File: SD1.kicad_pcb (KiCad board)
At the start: 2 copper layers, 76.2 x 38.1 mm, 145 parts, among them J101 HR861153C, J102 10118194-0001LF, J107 FPC PMS, J401 Conn_01x11, J403 FTDI_TTL_Cable, Q1 FDC2512, Q101 BSS138, Q102 PDTC114EU,115, SW103 Multidirection_Switch, SW104 Multifunction_Switch, SW401 PTS810, U101 TLV70233_SOT23-5, U102 ER-TFTM028-4, U103 CP2102N-A02-GQFN28R, U104 CC2652P, U105 W5500, U107 MCP23017, U3 TL431D, Y101 25MHz

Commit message: PoE layout
Changed opto and fixed ref diode footprint/symbol
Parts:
- removed C105, C106: 1u, Capacitor_SMD:C_0603_1608Metric
- removed D1, D2: MURA120, Diode_SMD:D_SMA
- removed R17: 39.2k, Resistor_SMD:R_0603_1608Metric
- removed R18: 392k, Resistor_SMD:R_0603_1608Metric
- removed SW104: Multifunction_Switch, mylib:K1-1508SA-01
- removed U101: TLV70233_SOT23-5, Package_TO_SOT_SMD:SOT-23-5
- removed U102: ER-TFTM028-4, mylib:ER-TFTM028-4
- added C109: 0.1u, Capacitor_SMD:C_0603_1608Metric, F.Cu at (132.9, 152.0)
- added C110: 0.1u, Capacitor_SMD:C_0603_1608Metric, F.Cu at (43.3, 117.8)
- added C112: 0.1u, Capacitor_SMD:C_0603_1608Metric, F.Cu at (43.3, 110.3)
- added C114: 10u, Capacitor_SMD:C_0603_1608Metric, F.Cu at (47.3, 113.7)
- added C301: 0.1u, Capacitor_SMD:C_0603_1608Metric, F.Cu at (55.4, 157.6)
- added C302: 0, Capacitor_SMD:C_0603_1608Metric, F.Cu at (52.0, 157.9)
- added C501: 1u, Capacitor_SMD:C_0603_1608Metric, F.Cu at (113.1, 155.3)
- added C502: 1u, Capacitor_SMD:C_0603_1608Metric, F.Cu at (113.6, 157.8)
- added C504: 0.1u, Capacitor_SMD:C_0603_1608Metric, F.Cu at (117.6, 156.6)
- added C505: 0.1u, Capacitor_SMD:C_0603_1608Metric, F.Cu at (113.6, 160.3)
- added C506: 10u, Capacitor_SMD:C_0603_1608Metric, F.Cu at (123.6, 152.0)
- added C507: 10u, Capacitor_SMD:C_0603_1608Metric, F.Cu at (117.6, 159.1)
- added C508: 1u, Capacitor_SMD:C_0603_1608Metric, F.Cu at (121.6, 156.6)
- added C601: 0.1u, Capacitor_SMD:C_0603_1608Metric, F.Cu at (31.0, 181.9)
- added C701: 10u, Capacitor_SMD:C_0603_1608Metric, F.Cu at (20.3, 148.4)
- added C704: 10u, Capacitor_SMD:C_0603_1608Metric, F.Cu at (16.3, 150.9)
- added C705: 10u, Capacitor_SMD:C_0603_1608Metric, F.Cu at (22.5, 144.8)
- added C706: 100p, Capacitor_SMD:C_0603_1608Metric, F.Cu at (16.3, 148.4)
- added C707: 47u, Capacitor_SMD:C_1210_3225Metric, F.Cu at (13.3, 143.6)
- added C708: 47u, Capacitor_SMD:C_1210_3225Metric, F.Cu at (11.5, 149.9)
- added C709: 100p, Capacitor_SMD:C_0603_1608Metric, F.Cu at (27.6, 135.5)
- added C710: 10u, Capacitor_SMD:C_0603_1608Metric, F.Cu at (31.6, 135.5)
- added C711: 10u, Capacitor_SMD:C_0603_1608Metric, F.Cu at (27.8, 138.0)
- added D3: BAS16, Diode_SMD:D_SOT-23_ANK, F.Cu at (228.2, 81.7)
- added D301: MURA120, Diode_SMD:D_SMA, F.Cu at (210.2, 25.1)
- added D302: MURA120, Diode_SMD:D_SMA, F.Cu at (214.7, 25.1)
- added D303: MURA120, Diode_SMD:D_SMA, F.Cu at (197.2, 25.2)
- added D304: MURA120, Diode_SMD:D_SMA, F.Cu at (201.0, 25.2)
- added D501: Photodiode alt, LED_THT:LED_D3.0mm_Clear, F.Cu at (107.4, 160.0)
- added D7: LED_ALT, LED_SMD:LED_0603_1608Metric, F.Cu at (261.6, 78.8)
- added D701: BAS16, Diode_SMD:D_SOT-23_ANK, F.Cu at (5.78, 149.4)
- added FB102: Ferrite_Bead_Small, Inductor_SMD:L_0603_1608Metric, F.Cu at (47.2, 106.2)
- added FB2: 10, Resistor_SMD:R_0603_1608Metric, F.Cu at (201.8, 76.6)
- added FB3: 10, Resistor_SMD:R_0603_1608Metric, F.Cu at (201.8, 81.8)
- added FB301: Ferrite_Bead_Small, Inductor_SMD:L_0603_1608Metric, F.Cu at (40.2, 135.5)
- added FB501: Ferrite_Bead_Small, Inductor_SMD:L_0603_1608Metric, F.Cu at (107.1, 187.4)
- added J103: JST ZH 1.5mm 1x5, mylib:JST-ZR-B5B-SM4-TFLFSN_1x05-1MP_P1.5mm_Vertical, F.Cu at (156.8, 143.0)
- added J301: PJ-102AH, Connector_BarrelJack:BarrelJack_CUI_PJ-102AH_Horizontal, F.Cu at (213.0, 19.2)
- added J302: PJ-102AH, Connector_BarrelJack:BarrelJack_CUI_PJ-102AH_Horizontal, F.Cu at (199.6, 19.0)
- added J303: Conn_01x02, Connector_PinSocket_2.54mm:PinSocket_1x02_P2.54mm_Vertical, F.Cu at (205.4, 69.0)
- added J304: Conn_01x02, Connector_PinSocket_2.54mm:PinSocket_1x02_P2.54mm_Vertical, F.Cu at (88.3, 107.2)
- added J402: Conn_ARM_JTAG_SWD_10, mylib:PinHeader_2x05_P1.27mm_Thin_Shrouded_Vertical_SMD, F.Cu at (57.6, 136.0)
- added J801: Conn_01x02, Connector_PinHeader_2.54mm:PinHeader_1x02_P2.54mm_Vertical, F.Cu at (12.8, 136.6)
- added JP301: Jumper_NO_Small, Jumper:SolderJumper-2_P1.3mm_Open_TrianglePad1.0x1.5mm, F.Cu at (263.6, 75.4)
- added JP401: Jumper_NO_Small, Connector_PinHeader_2.54mm:PinHeader_1x02_P2.54mm_Vertical, F.Cu at (64.8, 134.1)
- added JP701: Jumper_NO_Small, Jumper:SolderJumper-2_P1.3mm_Open_TrianglePad1.0x1.5mm, F.Cu at (18.3, 145.3)
- added JP702: Jumper_3_Bridged12, Jumper:SolderJumper-3_P1.3mm_Bridged12_Pad1.0x1.5mm, F.Cu at (17.9, 136.0)
- added L1: 4.7u, Inductor_SMD:L_Taiyo-Yuden_MD-4040, F.Cu at (218.3, 81.1)
- added L701: 1u, mylib:L_Wuerth_HCI-5040, F.Cu at (6.68, 144.4)
- added L702: 1u, mylib:L_Wuerth_HCI-5040, F.Cu at (6.68, 137.6)
- added Q301: DMMT5401, Package_TO_SOT_SMD:SOT-23-6, F.Cu at (267.4, 75.4)
- added Q302: DMMT5401, Package_TO_SOT_SMD:SOT-23-6, F.Cu at (267.4, 79.2)
- added Q801: DMMT5401, Package_TO_SOT_SMD:SOT-23-6, F.Cu at (23.2, 136.6)
- added Q802: DMMT5401, Package_TO_SOT_SMD:SOT-23-6, F.Cu at (18.5, 141.2)
- added Q803: DMMT5401, Package_TO_SOT_SMD:SOT-23-6, F.Cu at (23.4, 141.2)
- added R107: 47.5k, Resistor_SMD:R_0603_1608Metric, F.Cu at (95.3, 152.4)
- added R114: 10k, Resistor_SMD:R_0603_1608Metric, F.Cu at (47.3, 111.2)
- added R115: 10k, Resistor_SMD:R_0603_1608Metric, F.Cu at (43.3, 115.3)
- added R116: 10k, Resistor_SMD:R_0603_1608Metric, F.Cu at (43.3, 112.8)
- added R117: 10k, Resistor_SMD:R_0603_1608Metric, F.Cu at (47.3, 108.7)
- added R301: 0, Resistor_SMD:R_0603_1608Metric, F.Cu at (58.0, 152.4)
- added R302: 499k, Resistor_SMD:R_0603_1608Metric, F.Cu at (52.0, 160.4)
- added R303: 392k, Resistor_SMD:R_0603_1608Metric, F.Cu at (193.8, 22.2)
- added R304: 39.2k, Resistor_SMD:R_0603_1608Metric, F.Cu at (192.0, 20.6)
- added R305: 10k, Resistor_SMD:R_0603_1608Metric, F.Cu at (264.8, 78.8)
- added R306: 47.5k, Resistor_SMD:R_0603_1608Metric, F.Cu at (270.0, 78.8)
- added R307: 100k, Resistor_SMD:R_0603_1608Metric, F.Cu at (260.2, 82.0)
- added R308: 100k, Resistor_SMD:R_0603_1608Metric, F.Cu at (263.2, 82.0)
- added R501: 1M, Resistor_SMD:R_0603_1608Metric, F.Cu at (117.6, 161.6)
- added R601: 10k, Resistor_SMD:R_0603_1608Metric, F.Cu at (31.0, 184.4)
- added R602: 10k, Resistor_SMD:R_0603_1608Metric, F.Cu at (35.0, 181.9)
- added R603: 10k, Resistor_SMD:R_0603_1608Metric, F.Cu at (35.0, 184.4)
- added R702: 732k, Resistor_SMD:R_0603_1608Metric, F.Cu at (24.3, 149.8)
- added R703: 392k, Resistor_SMD:R_0603_1608Metric, F.Cu at (30.5, 143.1)
- added R704: 100k, Resistor_SMD:R_0603_1608Metric, F.Cu at (31.8, 140.5)
- added R705: 100k, Resistor_SMD:R_0603_1608Metric, F.Cu at (24.3, 147.3)
- added R801: 100k, Resistor_SMD:R_0603_1608Metric, F.Cu at (31.8, 138.0)
- added R802: 10k, Resistor_SMD:R_0603_1608Metric, F.Cu at (20.3, 150.9)
- added R803: 47.5k, Resistor_SMD:R_0603_1608Metric, F.Cu at (26.5, 144.8)
- added R804: 59k, Resistor_SMD:R_0603_1608Metric, F.Cu at (27.8, 140.5)
- added T1: HR051067, mylib:HR051067, F.Cu at (238.2, 75.4)
- added TP301: TestPoint, TestPoint:TestPoint_Pad_D1.0mm, F.Cu at (106.6, 196.5)
- added TP302: TestPoint, TestPoint:TestPoint_Pad_D1.0mm, F.Cu at (109.6, 196.5)
- added TP303: TestPoint, TestPoint:TestPoint_Pad_D1.0mm, F.Cu at (112.7, 196.5)
- added TP304: TestPoint, Connector_PinSocket_2.54mm:PinSocket_1x01_P2.54mm_Vertical, F.Cu at (258.7, 79.4)
- added TP501: TestPoint, TestPoint:TestPoint_Pad_D1.0mm, F.Cu at (106.6, 190.1)
- added TP502: TestPoint, TestPoint:TestPoint_Pad_D1.0mm, F.Cu at (110.6, 187.6)
- added U106: EKMC1691111, mylib:EKM, F.Cu at (84.2, 159.2)
- added U108: BME280, Package_LGA:Bosch_LGA-8_2.5x2.5mm_P0.65mm_ClockwisePinNumbering, F.Cu at (43.2, 107.0)
- added U109: SCD30, mylib:SCD30, F.Cu at (7.15, 106.9)
- added U2: TPS23753A, Package_SO:TSSOP-14_4.4x5mm_P0.65mm, B.Cu at (211.6, 73.6)
- added U301: 110-102, mylib:SPEC_110-102, F.Cu at (37.5, 163.7)
- added U302: LMP91000, Package_SON:WSON-14-1EP_4.0x4.0mm_P0.5mm_EP2.6x2.6mm, F.Cu at (53.0, 153.9)
- added U4: TCMT1107, Package_SO:SOIC-4_4.55x2.6mm_P1.27mm, F.Cu at (238.2, 67.0)
- added U501: TLV70018, Package_TO_SOT_SMD:SOT-353_SC-70-5, F.Cu at (119.1, 153.0)
- added U502: ADPD188BI, mylib:ADPD188BI, F.Cu at (108.4, 154.0)
- added U601: CCS811, Package_LGA:AMS_LGA-10-1EP_2.7x4mm_P0.6mm, F.Cu at (26.9, 183.4)
- added U701: TPS61022, mylib:Texas_VQFN-HR-7, F.Cu at (28.4, 147.8)
- added U702: TLV62585, Package_TO_SOT_SMD:SOT-563, F.Cu at (32.2, 145.9)
- C141: footprint Capacitor_SMD:C_1206_3216Metric -> Capacitor_SMD:C_0603_1608Metric
- C160: value 10n -> 8.2nF
- C24, C26, C32, C33, C34, C35, C36, C37, D6, R19, R20, R22, R23, R24, R25, R26, R27, R28, R29, R30, R32, R34, R35, R36, R37: moved to B.Cu
- FB101: value 470 -> Ferrite_Bead_Small
- Q1: value FDC2512 -> FDT86244; footprint Package_TO_SOT_SMD:SuperSOT-6 -> Package_TO_SOT_SMD:SOT-223-3_TabPin2
- R31: footprint Resistor_SMD:R_0805_2012Metric -> Resistor_SMD:R_0603_1608Metric
- U3: value TL431D -> TL431A; footprint Package_SO:SOIC-8_3.9x4.9mm_P1.27mm -> Package_TO_SOT_SMD:SOT-23; moved to B.Cu
- moved C28 107.2 mm to (259.2, 74.0), turned to 90 degrees
- moved D4 96.6 mm to (251.6, 78.6), turned to 180 degrees
- moved C35 95.8 mm to (253.8, 75.3), turned to 180 degrees
- moved C29 95.3 mm to (251.8, 72.7), turned to 90 degrees
- moved D6 95.1 mm to (249.0, 74.8), turned to 180 degrees
- moved R26 94.3 mm to (232.1, 74.4)
- moved U3 93.0 mm to (253.6, 71.1)
- moved C33 90.2 mm to (253.8, 73.8), turned to 180 degrees
- moved R27 89.0 mm to (249.2, 77.4), turned to 180 degrees
- moved R37 86.2 mm to (256.1, 70.8), turned to 90 degrees
- moved R24 85.2 mm to (256.1, 76.8), turned to 270 degrees
- moved C24 84.7 mm to (253.4, 79.4), turned to 180 degrees
- moved C27 83.0 mm to (255.0, 72.7), turned to 90 degrees
- moved C32 81.0 mm to (233.6, 71.8), turned to 180 degrees
- moved R31 77.7 mm to (263.2, 78.8), turned to 270 degrees
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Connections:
- net /Eth + PoE/PoE Flyback/5V_SYS renamed /Eth + PoE/PoE Flyback/5V_Main
- net /WMCU_SWO renamed /WMCU_RTS
- C23 pad 1: (no net) -> Net-(C23-Pad1)
- J107 pad 3: (no net) -> /EXT_Sleep
- J107 pad 4: (no net) -> I2C_SCL
- J107 pad 5: (no net) -> I2C_SDA
- J403 pad 3: (no net) -> Net-(J403-Pad3)
- LS101 pad 1: /5V_USB -> +3V3
- Q1 pad 2: Net-(Q1-Pad1) -> Net-(Q1-Pad2)
- R108 pad 2: /5V_USB -> +3V3
- R111 pad 1: (no net) -> /I_LED_R
- R112 pad 1: (no net) -> /I_LED_G
- R113 pad 1: (no net) -> /I_LED_B
- R19 pad 2: (no net) -> Net-(R19-Pad2)
- R21 pad 1: (no net) -> Net-(R21-Pad1)
- R21 pad 2: (no net) -> Net-(D3-Pad2)
- R22 pad 1: (no net) -> Net-(J303-Pad2)
- R23 pad 1: (no net) -> Net-(R23-Pad1)
- R25 pad 1: Net-(Q1-Pad3) -> Net-(Q1-Pad1)
- R25 pad 2: (no net) -> Net-(R25-Pad2)
- R26 pad 1: Net-(Q1-Pad1) -> Net-(Q1-Pad2)
- R27 pad 2: (no net) -> Net-(R27-Pad2)
- R30 pad 1: Net-(Q1-Pad4) -> Net-(Q1-Pad3)
- R30 pad 2: (no net) -> Net-(R30-Pad2)
- R31 pad 2: (no net) -> Net-(D7-Pad2)
- R32 pad 1: (no net) -> Net-(R32-Pad1)
- R33 pad 1: Net-(Q1-Pad4) -> Net-(Q1-Pad3)
- SW103 pad 1: (no net) -> /Multi_A
- SW103 pad 2: (no net) -> /Multi_B
- SW103 pad 3: (no net) -> /Multi_C
- SW103 pad 4: (no net) -> /Multi_Press
- SW103 pad 5: (no net) -> GND
- SW103 pad 6: (no net) -> /Multi_D
- U103 pad 25: /DIO13_TXD -> /DIO12_RXD
- U103 pad 26: /DIO12_RXD -> /DIO13_TXD
- U104 pad 1: (no net) -> I2C_SDA
- U104 pad 14: (no net) -> GND
- U104 pad 16: /DIO16_TDO -> (no net)
- U104 pad 17: /DIO17_TDI -> /DIO16_TDO
- U104 pad 18: (no net) -> /DIO17_TDI
- U104 pad 21: (no net) -> I2C_SCL
- U104 pad 24: (no net) -> /CO_ADC
- U104 pad 25: (no net) -> 5V_MainDet
- U104 pad 4: (no net) -> SPI_MISO
- U104 pad 5: (no net) -> SPI_MOSI
- U104 pad 6: (no net) -> SPI_SCK
- U105 pad 37: (no net) -> /~ETH_RST
- U107 pad 12: (no net) -> I2C_SCL
- U107 pad 13: (no net) -> I2C_SDA
- U107 pad 21: (no net) -> /I_LED_R
- U107 pad 22: (no net) -> /I_LED_G
- U107 pad 23: (no net) -> /I_LED_B
- U107 pad 24: (no net) -> /Multi_A
- U107 pad 25: (no net) -> /Multi_B
- U107 pad 26: (no net) -> /Multi_C
- U107 pad 27: (no net) -> /Multi_D
- U107 pad 28: (no net) -> /Multi_Press
- U107 pad 3: (no net) -> /LCD_DC
- U107 pad 4: (no net) -> /FONT_CS
- U107 pad 6: (no net) -> /~ETH_RST
- U107 pad 7: (no net) -> /VOC_INT
- U107 pad 8: (no net) -> /EXT_Sleep
- U3 pad 2: GND -> Net-(C33-Pad1)
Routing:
- net GNDD: track 0.00 -> 104.7 mm, vias 0 -> 21
- net GND: track 55.4 -> 114.0 mm, vias 8 -> 10
- net Net-(C37-Pad2): track 0.00 -> 26.1 mm, vias 0 -> 1
- net Net-(C21-Pad1): track 0.00 -> 25.6 mm, vias 0 -> 1
- net /Eth + PoE/PoE Flyback/VSS_FILT: track 0.00 -> 22.9 mm, vias 0 -> 2
- net Net-(C25-Pad1): track 0.00 -> 20.8 mm, vias 0 -> 1
- net +5V: track 0.00 -> 20.0 mm
- net Net-(C33-Pad2): track 0.00 -> 19.7 mm, vias 0 -> 1
- net /Eth + PoE/PoE Flyback/5V_Main: track 0.00 -> 18.4 mm, vias 0 -> 2
- net Net-(C23-Pad1): track 0.00 -> 16.3 mm
- net Net-(Q1-Pad1): track 0.00 -> 14.7 mm, vias 0 -> 1
- net Net-(R27-Pad2): track 0.00 -> 14.2 mm, vias 0 -> 1
- net Net-(D6-Pad2): track 0.00 -> 13.9 mm
- net 5V_MainDet: track 0.00 -> 13.6 mm
- net /Eth + PoE/PoE Flyback/VP: track 13.1 -> 25.9 mm
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- added copper zone on F.Cu, net /Eth + PoE/PoE Flyback/5V_Main
- added copper zone on B.Cu, net /Eth + PoE/PoE Flyback/VSS_FILT
- added copper zone on B.Cu, net GNDD
- added copper zone on F.Cu, net GNDD
- added copper zone on B.Cu, net Net-(C21-Pad1)
- added copper zone on F.Cu, net Net-(C21-Pad1)
- added copper zone on F.Cu, net Net-(C23-Pad1)
- added copper zone on F.Cu, net Net-(D4-Pad2)
- added copper zone on F.Cu, net Net-(JP301-Pad2)
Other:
- board size 76.2 x 38.1 mm -> 176.1 x 41.3 mm

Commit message: Layout for Smoke and Reference Indicators for PoE
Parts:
- C501, C502, FB501, U501: moved to B.Cu
- moved FB501 147.7 mm to (54.5, 49.4), turned to 180 degrees
- moved D501 141.5 mm to (41.9, 34.6)
- moved TP501 139.0 mm to (75.7, 54.6)
- moved TP502 135.3 mm to (75.7, 56.9)
- moved C505 127.7 mm to (54.7, 47.0)
- moved C507 126.2 mm to (49.1, 53.1), turned to 180 degrees
- moved C504 125.0 mm to (54.7, 48.6)
- moved C508 124.9 mm to (55.9, 50.4)
- moved R501 124.0 mm to (58.8, 52.5)
- moved C506 122.5 mm to (49.1, 54.6), turned to 180 degrees
- moved C502 120.4 mm to (56.8, 51.7), turned to 90 degrees
- moved U501 120.3 mm to (54.4, 51.7)
- moved C501 120.2 mm to (51.9, 51.8), turned to 90 degrees
- moved U502 113.4 mm to (54.6, 54.1)
- moved C401 57.3 mm to (98.8, 88.1), turned to 180 degrees
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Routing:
- net GND: track 114.0 -> 145.5 mm, vias 10 -> 12
- net Net-(D501-Pad1): track 0.00 -> 23.4 mm
- net Net-(D501-Pad2): track 0.00 -> 21.1 mm
- net Net-(TP502-Pad1): track 0.00 -> 20.2 mm
- net Net-(TP501-Pad1): track 0.00 -> 19.8 mm
- net +3V3: track 46.3 -> 65.3 mm, vias 2 -> 3
- net +5V: track 20.0 -> 33.8 mm
- net Net-(C504-Pad1): track 0.00 -> 11.0 mm, vias 0 -> 1
- net +1V8: track 0.00 -> 9.43 mm, vias 0 -> 1
- net Net-(R501-Pad1): track 0.00 -> 1.82 mm
- net Net-(C508-Pad1): track 0.00 -> 1.70 mm

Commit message: Modified layout for Smoke, Fixed Ideal Diode
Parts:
- removed Q803: DMMT5401, Package_TO_SOT_SMD:SOT-23-6
- added U102: ER-TFTM028-4, mylib:ER-TFTM028-4, F.Cu at (351.1, 48.6)
- moved L702 293.8 mm to (276.3, 20.8)
- moved C701 279.1 mm to (272.8, 29.5), turned to 270 degrees
- moved C708 277.7 mm to (269.4, 47.1), turned to 270 degrees
- moved R705 276.6 mm to (274.6, 29.5), turned to 90 degrees
- moved D701 275.6 mm to (259.4, 41.7)
- moved C711 271.4 mm to (277.0, 30.6), turned to 180 degrees
- moved C707 270.6 mm to (266.0, 47.1), turned to 270 degrees
- moved U702 270.4 mm to (274.2, 25.2), turned to 270 degrees
- moved R703 270.4 mm to (277.1, 32.2), turned to 180 degrees
- moved C709 269.4 mm to (277.1, 33.9), turned to 180 degrees
- moved R804 269.1 mm to (274.5, 33.1), turned to 270 degrees
- moved C706 268.1 mm to (263.6, 44.7), turned to 90 degrees
- moved C710 267.6 mm to (277.0, 28.9), turned to 180 degrees
- moved L701 265.7 mm to (255.5, 51.4)
- moved JP701 264.4 mm to (259.5, 37.2), turned to 180 degrees
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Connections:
- J102 pad 4: (no net) -> Net-(J102-Pad4)
- J107 pad 1: (no net) -> Net-(J107-Pad1)
- J107 pad 6: (no net) -> Net-(J107-Pad6)
- J107 pad 7: (no net) -> Net-(J107-Pad7)
- J107 pad 8: (no net) -> Net-(J107-Pad8)
- J401 pad 2: (no net) -> /DB_5V
- J402 pad 7: (no net) -> Net-(J402-Pad7)
- Q102 pad 1: (no net) -> /SPKR_Alt
- Q802 pad 3: (no net) -> Net-(Q802-Pad1)
- Q802 pad 4: (no net) -> Net-(Q801-Pad1)
- Q802 pad 5: (no net) -> +5V
- R109 pad 1: (no net) -> /SPKR
- U103 pad 1: (no net) -> Net-(U103-Pad1)
- U103 pad 10: (no net) -> Net-(U103-Pad10)
- U103 pad 11: (no net) -> Net-(U103-Pad11)
- U103 pad 12: (no net) -> Net-(U103-Pad12)
- U103 pad 13: (no net) -> Net-(U103-Pad13)
- U103 pad 14: (no net) -> Net-(U103-Pad14)
- U103 pad 15: (no net) -> Net-(U103-Pad15)
- U103 pad 16: (no net) -> Net-(U103-Pad16)
- U103 pad 17: (no net) -> Net-(U103-Pad17)
- U103 pad 2: (no net) -> Net-(U103-Pad2)
- U103 pad 21: (no net) -> Net-(U103-Pad21)
- U103 pad 22: (no net) -> Net-(U103-Pad22)
- U103 pad 27: (no net) -> Net-(U103-Pad27)
- U103 pad 28: (no net) -> Net-(U103-Pad28)
- U104 pad 15: (no net) -> Net-(U104-Pad15)
- U104 pad 16: (no net) -> Net-(U104-Pad16)
- U104 pad 2: (no net) -> Net-(U104-Pad2)
- U104 pad 20: (no net) -> /WMCU_CTS
- U104 pad 22: (no net) -> Net-(U104-Pad22)
- U104 pad 23: (no net) -> Net-(U104-Pad23)
- U104 pad 26: (no net) -> Net-(U104-Pad26)
- U104 pad 27: (no net) -> Net-(U104-Pad27)
- U104 pad 28: (no net) -> Net-(U104-Pad28)
- U104 pad 29: (no net) -> Net-(U104-Pad29)
- U104 pad 3: (no net) -> Net-(U104-Pad3)
- U104 pad 30: (no net) -> Net-(U104-Pad30)
- U104 pad 7: (no net) -> Net-(U104-Pad7)
- U105 pad 12: (no net) -> Net-(U105-Pad12)
- U105 pad 13: (no net) -> Net-(U105-Pad13)
- U105 pad 18: (no net) -> Net-(U105-Pad18)
- U105 pad 24: (no net) -> /Eth + PoE/SPD_LED
- U105 pad 26: (no net) -> /Eth + PoE/DUP_LED
- U105 pad 32: (no net) -> /ETH_CS
- U105 pad 36: (no net) -> /~ETH_INT
- U105 pad 46: (no net) -> Net-(U105-Pad46)
- U105 pad 47: (no net) -> Net-(U105-Pad47)
- U105 pad 7: (no net) -> Net-(U105-Pad7)
- U107 pad 1: (no net) -> Net-(U107-Pad1)
- U107 pad 11: (no net) -> Net-(U107-Pad11)
- U107 pad 14: (no net) -> Net-(U107-Pad14)
- U107 pad 19: (no net) -> Net-(U107-Pad19)
- U107 pad 2: (no net) -> /EN_5V_BST
- U107 pad 20: (no net) -> /IO_INT
- U107 pad 5: (no net) -> /LCD_RESET
- U109 pad 5: (no net) -> Net-(U109-Pad5)
- U109 pad 6: (no net) -> Net-(U109-Pad6)
- U302 pad 5: (no net) -> Net-(U302-Pad5)
- U501 pad 4: (no net) -> GND
- U502 pad 10: (no net) -> Net-(U502-Pad10)
- U502 pad 16: (no net) -> Net-(U502-Pad16)
- U502 pad 2: (no net) -> Net-(U502-Pad2)
- U502 pad 3: (no net) -> Net-(U502-Pad3)
- U502 pad 7: (no net) -> Net-(U502-Pad7)
- U502 pad 8: (no net) -> Net-(U502-Pad8)
- U502 pad 9: (no net) -> Net-(U502-Pad9)
- U601 pad 8: (no net) -> Net-(U601-Pad8)
- U702 pad 6: (no net) -> Net-(U702-Pad6)
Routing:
- net /PIR_SENSE: track 0.00 -> 11.5 mm
- net +3V3: track 65.3 -> 74.7 mm
- net GND: track 145.5 -> 154.9 mm
- net Net-(D501-Pad2): track 21.1 -> 12.1 mm
- net Net-(D501-Pad1): track 23.4 -> 14.5 mm
- net Net-(TP501-Pad1): track 19.8 -> 12.2 mm
- net Net-(TP502-Pad1): track 20.2 -> 12.9 mm
- net I2C_SDA: track 6.10 -> 12.9 mm
- net I2C_SCL: track 4.70 -> 11.2 mm
- net +5V: track 33.8 -> 29.8 mm
- net Net-(C508-Pad1): track 1.70 -> 3.41 mm
- net Net-(C504-Pad1): track 11.0 -> 9.91 mm

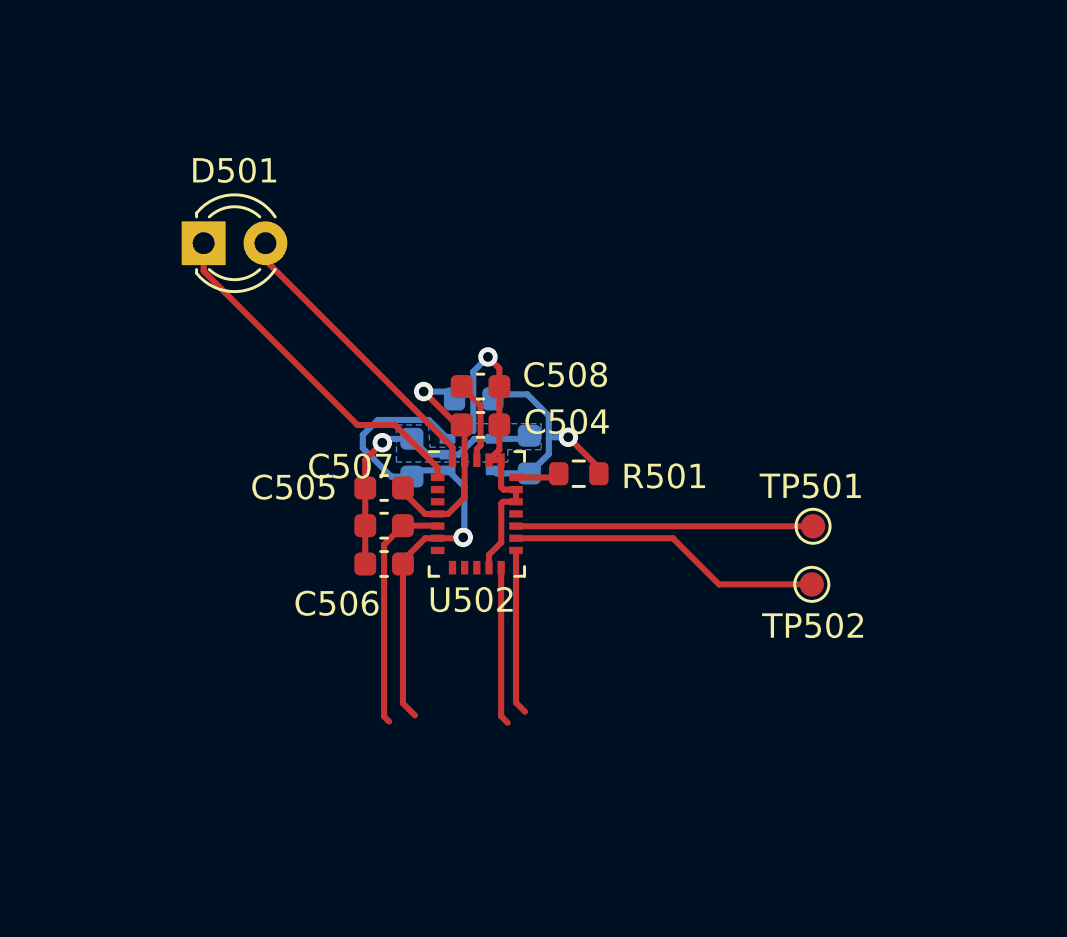
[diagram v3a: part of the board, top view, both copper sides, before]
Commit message: Add smoke chamber to sch and layout
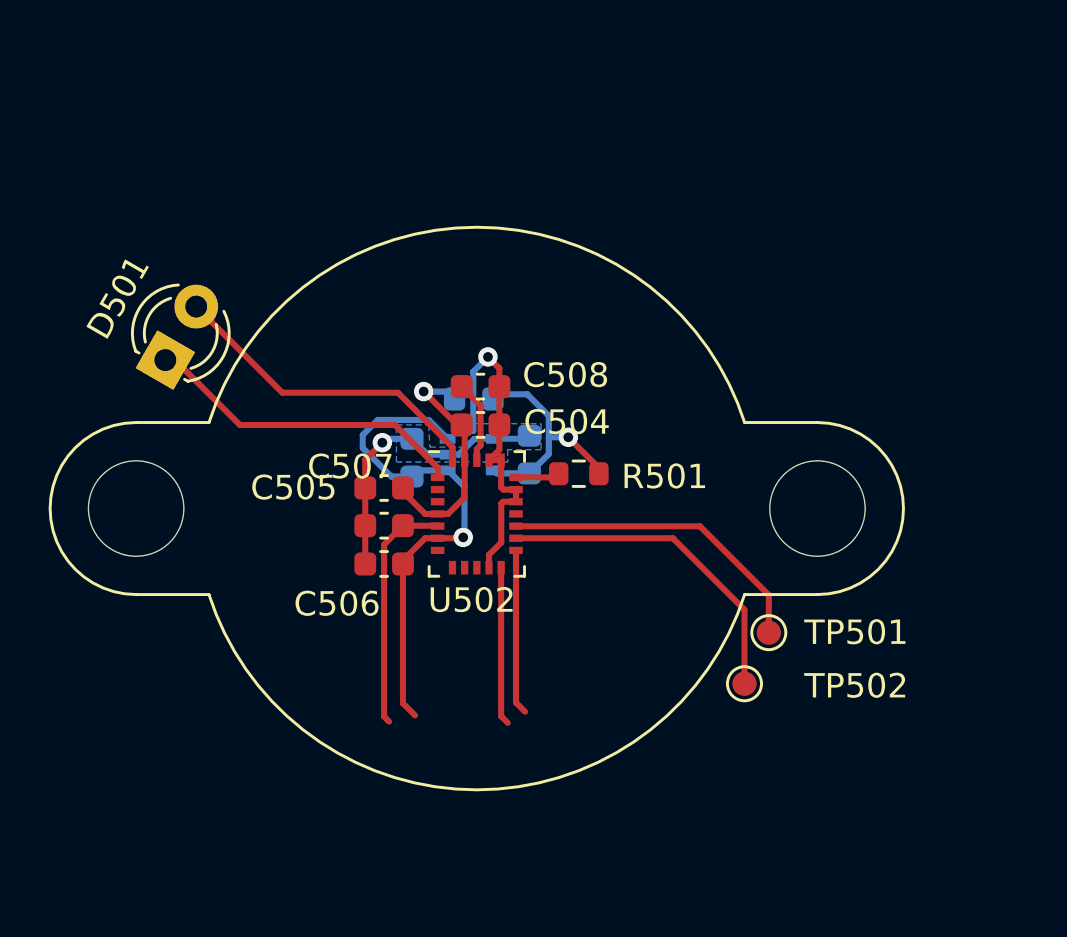
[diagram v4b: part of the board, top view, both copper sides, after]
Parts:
- added U503: Smoke Chamber, mylib:ADPD188BI_Chamber, F.Cu at (31.8, 29.7)
- moved D501 5.06 mm to (19.0, 23.6), turned to 60 degrees
- moved TP502 4.93 mm to (42.8, 36.9)
- moved TP501 4.73 mm to (43.8, 34.8)
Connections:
- J102 pad 4: Net-(J102-Pad4) -> (no net)
- J107 pad 1: Net-(J107-Pad1) -> (no net)
- J107 pad 6: Net-(J107-Pad6) -> (no net)
- J107 pad 7: Net-(J107-Pad7) -> (no net)
- J107 pad 8: Net-(J107-Pad8) -> (no net)
- J401 pad 2: /DB_5V -> (no net)
- J402 pad 7: Net-(J402-Pad7) -> (no net)
- Q102 pad 1: /SPKR_Alt -> (no net)
- R109 pad 1: /SPKR -> (no net)
- U102 pad 10: Net-(U102-Pad10) -> (no net)
- U102 pad 11: Net-(U102-Pad11) -> (no net)
- U102 pad 12: Net-(U102-Pad12) -> (no net)
- U102 pad 13: Net-(U102-Pad13) -> (no net)
- U102 pad 14: Net-(U102-Pad14) -> (no net)
- U102 pad 15: Net-(U102-Pad15) -> (no net)
- U102 pad 16: Net-(U102-Pad16) -> (no net)
- U102 pad 17: Net-(U102-Pad17) -> (no net)
- U102 pad 18: Net-(U102-Pad18) -> (no net)
- U102 pad 19: Net-(U102-Pad19) -> (no net)
- U102 pad 20: Net-(U102-Pad20) -> (no net)
- U102 pad 21: /~LCD_RESET -> (no net)
- U102 pad 22: Net-(U102-Pad22) -> (no net)
- U102 pad 23: /~LCD_CS -> (no net)
- U102 pad 29: /LCD_BACKLIGHT -> (no net)
- U102 pad 3: Net-(U102-Pad3) -> (no net)
- U102 pad 35: /SD_CS -> (no net)
- U102 pad 37: Net-(U102-Pad37) -> (no net)
- U102 pad 38: Net-(U102-Pad38) -> (no net)
- U102 pad 39: /CTP_INT -> (no net)
- U102 pad 4: Net-(U102-Pad4) -> (no net)
- U102 pad 41: Net-(U102-Pad41) -> (no net)
- U102 pad 42: Net-(U102-Pad42) -> (no net)
- U102 pad 43: Net-(U102-Pad43) -> (no net)
- U102 pad 44: Net-(U102-Pad44) -> (no net)
- U102 pad 5: Net-(U102-Pad5) -> (no net)
- U102 pad 6: Net-(U102-Pad6) -> (no net)
- U102 pad 7: Net-(U102-Pad7) -> (no net)
- U102 pad 8: Net-(U102-Pad8) -> (no net)
- U102 pad 9: Net-(U102-Pad9) -> (no net)
- U103 pad 1: Net-(U103-Pad1) -> (no net)
- U103 pad 10: Net-(U103-Pad10) -> (no net)
- U103 pad 11: Net-(U103-Pad11) -> (no net)
- U103 pad 12: Net-(U103-Pad12) -> (no net)
- U103 pad 13: Net-(U103-Pad13) -> (no net)
- U103 pad 14: Net-(U103-Pad14) -> (no net)
- U103 pad 15: Net-(U103-Pad15) -> (no net)
- U103 pad 16: Net-(U103-Pad16) -> (no net)
- U103 pad 17: Net-(U103-Pad17) -> (no net)
- U103 pad 2: Net-(U103-Pad2) -> (no net)
- U103 pad 21: Net-(U103-Pad21) -> (no net)
- U103 pad 22: Net-(U103-Pad22) -> (no net)
- U103 pad 27: Net-(U103-Pad27) -> (no net)
- U103 pad 28: Net-(U103-Pad28) -> (no net)
- U104 pad 15: Net-(U104-Pad15) -> (no net)
- U104 pad 16: Net-(U104-Pad16) -> (no net)
- U104 pad 2: Net-(U104-Pad2) -> (no net)
- U104 pad 20: /WMCU_CTS -> (no net)
- U104 pad 22: Net-(U104-Pad22) -> (no net)
- U104 pad 23: Net-(U104-Pad23) -> (no net)
- U104 pad 26: Net-(U104-Pad26) -> (no net)
- U104 pad 27: Net-(U104-Pad27) -> (no net)
- U104 pad 28: Net-(U104-Pad28) -> (no net)
- U104 pad 29: Net-(U104-Pad29) -> (no net)
- U104 pad 3: Net-(U104-Pad3) -> (no net)
- U104 pad 30: Net-(U104-Pad30) -> (no net)
- U104 pad 7: Net-(U104-Pad7) -> (no net)
- U105 pad 12: Net-(U105-Pad12) -> (no net)
- U105 pad 13: Net-(U105-Pad13) -> (no net)
- U105 pad 18: Net-(U105-Pad18) -> (no net)
- U105 pad 24: /Eth + PoE/SPD_LED -> (no net)
- U105 pad 26: /Eth + PoE/DUP_LED -> (no net)
- U105 pad 32: /ETH_CS -> (no net)
- U105 pad 36: /~ETH_INT -> (no net)
- U105 pad 46: Net-(U105-Pad46) -> (no net)
- U105 pad 47: Net-(U105-Pad47) -> (no net)
- U105 pad 7: Net-(U105-Pad7) -> (no net)
- U107 pad 1: Net-(U107-Pad1) -> (no net)
- U107 pad 11: Net-(U107-Pad11) -> (no net)
- U107 pad 14: Net-(U107-Pad14) -> (no net)
- U107 pad 19: Net-(U107-Pad19) -> (no net)
- U107 pad 2: /EN_5V_BST -> (no net)
- U107 pad 20: /IO_INT -> (no net)
- U107 pad 5: /LCD_RESET -> (no net)
- U109 pad 5: Net-(U109-Pad5) -> (no net)
- U109 pad 6: Net-(U109-Pad6) -> (no net)
- U302 pad 5: Net-(U302-Pad5) -> (no net)
- U501 pad 4: GND -> (no net)
- U502 pad 10: Net-(U502-Pad10) -> (no net)
- U502 pad 16: Net-(U502-Pad16) -> (no net)
- U502 pad 2: Net-(U502-Pad2) -> (no net)
- U502 pad 3: Net-(U502-Pad3) -> (no net)
- U502 pad 7: Net-(U502-Pad7) -> (no net)
- U502 pad 8: Net-(U502-Pad8) -> (no net)
- U502 pad 9: Net-(U502-Pad9) -> (no net)
- U601 pad 8: Net-(U601-Pad8) -> (no net)
- U702 pad 6: Net-(U702-Pad6) -> (no net)
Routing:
- net Net-(D501-Pad2): track 12.1 -> 13.5 mm
- net Net-(D501-Pad1): track 14.5 -> 13.4 mm
- net Net-(TP501-Pad1): track 12.2 -> 13.1 mm
- net Net-(TP502-Pad1): track 12.9 -> 13.6 mm
